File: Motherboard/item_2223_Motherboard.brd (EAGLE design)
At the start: 160 x 100 mm, 50 parts, among them IC1 MCP602SN, IC2 LD117AS33TR, IC4 MCP6S26, U1 ESP32-DEVKITC-32D, U2 ADS1256_BOARD, U3 SSD1306_128X64, X1 MSTBA4, X2 MSTBA4

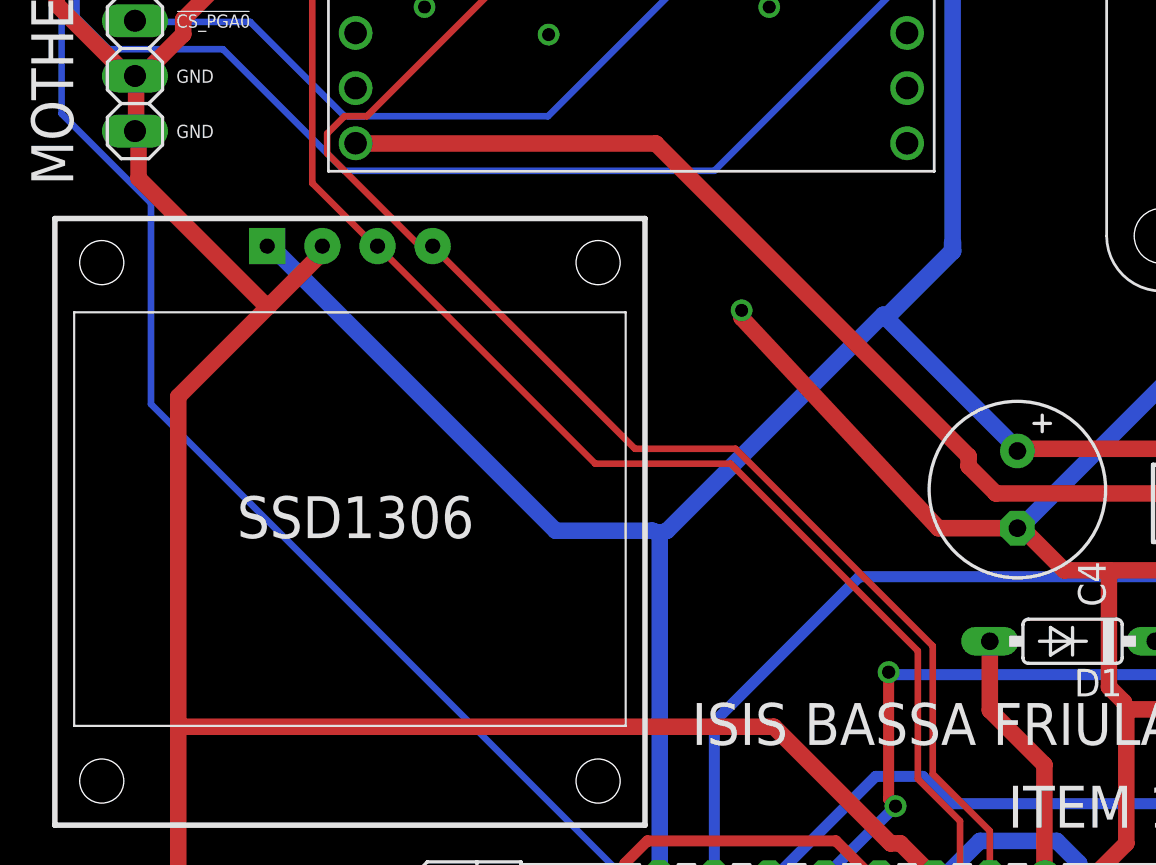
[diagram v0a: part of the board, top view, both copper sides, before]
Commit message: Corretto GND di SSD1306 in Frontend e Motherboard
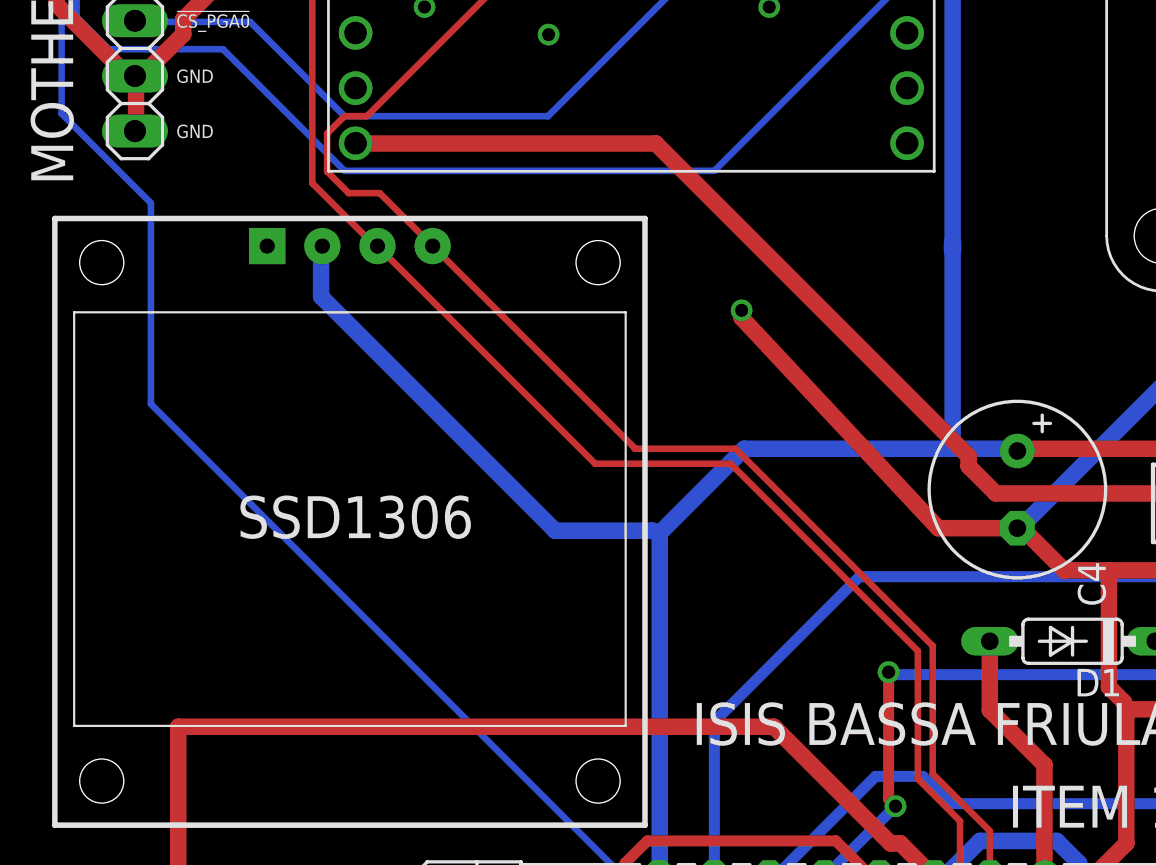
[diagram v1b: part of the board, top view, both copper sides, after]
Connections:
- net +3V3: now also U3.2; no longer U3.VCC
- net GND: now also U3.1; no longer U3.GND
- net I2C_SCL: now also U3.3; no longer U3.SCL
- net I2C_SDA: now also U3.4; no longer U3.SDA
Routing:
- net GND: track 792.6 -> 757.4 mm
- net +3V3: track 249.1 -> 247.7 mm
- net I2C_SDA: track 94.1 -> 94.6 mm
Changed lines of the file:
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@@
 <?xml version="1.0" encoding="utf-8"?>
 <!DOCTYPE eagle SYSTEM "eagle.dtd">
-<eagle version="9.6.2">
+<eagle version="7.7.0">
 <drawing>
 <settings>
 <setting alwaysvectorfont="no"/>
-<setting keepoldvectorfont="yes"/>
 <setting verticaltext="up"/>
 </settings>
@@
 <param name="dpMaxLengthDifference" value="10mm"/>
 <param name="dpGapFactor" value="2.5"/>
+<param name="checkGrid" value="0"/>
 <param name="checkAngle" value="0"/>
 <param name="checkFont" value="1"/>
 <param name="checkRestrict" value="1"/>
-<param name="checkStop" value="0"/>
-<param name="checkValues" value="0"/>
-<param name="checkNames" value="1"/>
-<param name="checkWireStubs" value="1"/>
-<param name="checkPolygonWidth" value="0"/>
 <param name="useDiameter" value="13"/>
 <param name="maxErrors" value="50"/>
@@
 <contactref element="RTD1" pad="P3"/>
 <contactref element="RTD2" pad="P3"/>
-<contactref element="U3" pad="VCC"/>
+<contactref element="U3" pad="2"/>
 <contactref element="JP1" pad="2"/>
 <contactref element="IC2" pad="4"/>
@@
 <wire x1="30.5181" y1="27.2034" x2="30.5181" y2="11.43" width="0.762" layer="16"/>
 <wire x1="30.5181" y1="11.43" x2="30.48" y2="11.43" width="0.762" layer="16"/>
-<wire x1="12.6873" y1="40.3479" x2="12.4587" y2="40.3479" width="0.762" layer="16"/>
-<wire x1="25.7175" y1="27.3177" x2="12.6873" y2="40.3479" width="0.762" layer="16"/>
-<wire x1="30.1752" y1="27.3177" x2="25.7175" y2="27.3177" width="0.762" layer="16"/>
-<wire x1="12.4587" y1="40.3479" x2="12.44" y2="40.425" width="0.762" layer="16"/>
+<wire x1="30.1752" y1="27.3177" x2="25.7048" y2="27.3177" width="0.762" layer="16"/>
 <wire x1="30.1752" y1="27.3177" x2="30.5181" y2="27.2034" width="0.762" layer="16"/>
 <wire x1="133.6167" y1="94.5261" x2="133.6167" y2="94.9833" width="0.762" layer="16"/>
@@
 <via x="128.8161" y="89.7255" extent="1-16" drill="0.6096"/>
 <via x="71.2089" y="90.4113" extent="1-16" drill="0.6096"/>
-<wire x1="30.861" y1="27.3177" x2="40.8051" y2="37.2618" width="0.762" layer="16"/>
-<wire x1="30.861" y1="27.3177" x2="30.5181" y2="27.2034" width="0.762" layer="16"/>
-<wire x1="40.8051" y1="37.2618" x2="40.93845" y2="37.12845" width="0.762" layer="16"/>
-<wire x1="40.93845" y1="37.12845" x2="46.9773" y2="31.0896" width="0.762" layer="16"/>
 <wire x1="46.9773" y1="31.0896" x2="46.99" y2="30.988" width="0.762" layer="16"/>
 <wire x1="56.5785" y1="31.7754" x2="66.6369" y2="31.7754" width="0.762" layer="1"/>
@@
 <wire x1="56.2356" y1="31.5468" x2="56.515" y2="31.725" width="0.762" layer="1"/>
 <wire x1="44.0055" y1="40.5892" x2="44.0055" y2="40.1955" width="0.8128" layer="16"/>
-<wire x1="44.0055" y1="40.1955" x2="40.93845" y2="37.12845" width="0.8128" layer="16"/>
 <contactref element="IC4" pad="14"/>
 <contactref element="C10" pad="1"/>
@@
 <wire x1="80.01" y1="30.21" x2="83.55" y2="30.21" width="0.762" layer="1"/>
 <wire x1="83.55" y1="30.21" x2="85.09" y2="31.75" width="0.762" layer="1"/>
+<wire x1="25.7048" y1="27.3177" x2="14.9225" y2="38.1" width="0.762" layer="16"/>
+<wire x1="14.9225" y1="38.1" x2="14.9225" y2="40.3675" width="0.762" layer="16"/>
+<wire x1="14.9225" y1="40.3675" x2="14.98" y2="40.425" width="0.762" layer="16"/>
+<wire x1="46.9773" y1="31.0896" x2="44.1325" y2="31.0896" width="0.762" layer="16"/>
+<wire x1="44.1325" y1="31.0896" x2="34.4043" y2="31.0896" width="0.762" layer="16"/>
+<wire x1="34.4043" y1="31.0896" x2="30.5181" y2="27.2034" width="0.762" layer="16"/>
+<wire x1="44.0055" y1="40.1955" x2="44.0055" y2="31.2166" width="0.762" layer="16"/>
+<wire x1="44.0055" y1="31.2166" x2="44.1325" y2="31.0896" width="0.762" layer="16"/>
 <wire x1="85.09" y1="31.75" x2="85.09" y2="32.2834" width="0" layer="19" extent="1-1"/>
 </signal>
@@
 <contactref element="U1" pad="26"/>
 <contactref element="U1" pad="20"/>
-<contactref element="U3" pad="GND"/>
+<contactref element="U3" pad="1"/>
 <contactref element="JP1" pad="4"/>
 <contactref element="C3" pad="2"/>
@@
 <contactref element="PL1" pad="5"/>
 <contactref element="PL1" pad="14"/>
-<wire x1="8.3439" y1="33.4899" x2="8.3439" y2="18.288" width="0.762" layer="1"/>
 <wire x1="8.3439" y1="18.288" x2="8.3439" y2="9.6012" width="0.762" layer="1"/>
-<wire x1="14.9733" y1="40.1193" x2="12.4587" y2="37.6047" width="0.762" layer="1"/>
-<wire x1="12.4587" y1="37.6047" x2="8.3439" y2="33.4899" width="0.762" layer="1"/>
-<wire x1="14.9733" y1="40.3479" x2="14.9733" y2="40.1193" width="0.762" layer="1"/>
 <wire x1="8.3439" y1="9.6012" x2="8.255" y2="9.525" width="0.762" layer="1"/>
-<wire x1="14.9733" y1="40.3479" x2="14.98" y2="40.425" width="0.762" layer="1"/>
 <wire x1="41.9481" y1="76.1238" x2="41.9481" y2="75.6666" width="0.762" layer="1"/>
 <wire x1="43.5483" y1="77.724" x2="41.9481" y2="76.1238" width="0.762" layer="1"/>
@@
 <wire x1="41.6052" y1="75.438" x2="41.91" y2="75.64" width="0.762" layer="1"/>
 <wire x1="16.8021" y1="58.0644" x2="16.51" y2="57.86" width="0.762" layer="1"/>
-<wire x1="6.5151" y1="43.5483" x2="12.4587" y2="37.6047" width="0.762" layer="1"/>
-<wire x1="6.5151" y1="45.3771" x2="6.5151" y2="43.5483" width="0.762" layer="1"/>
 <wire x1="6.5151" y1="45.3771" x2="6.35" y2="45.72" width="0.762" layer="1"/>
 <wire x1="106.299" y1="95.5548" x2="106.0704" y2="95.5548" width="0.762" layer="16"/>
@@
 <signal name="I2C_SCL" class="2">
 <contactref element="U1" pad="22"/>
-<contactref element="U3" pad="SCL"/>
+<contactref element="U3" pad="3"/>
 <contactref element="PL1" pad="4"/>
 <wire x1="45.72" y1="9.7155" x2="45.72" y2="8.89" width="0.3048" layer="1"/>
@@
 <wire x1="42.4053" y1="21.7805" x2="42.4053" y2="15.8877" width="0.3048" layer="1"/>
 <wire x1="33.782" y1="30.4038" x2="42.4053" y2="21.7805" width="0.3048" layer="1"/>
-<wire x1="27.5463" y1="30.4038" x2="33.782" y2="30.4038" width="0.3048" layer="1"/>
-<wire x1="17.6022" y1="40.3479" x2="27.5463" y2="30.4038" width="0.3048" layer="1"/>
-<wire x1="17.6022" y1="40.3479" x2="17.52" y2="40.425" width="0.3048" layer="1"/>
+<wire x1="27.5412" y1="30.4038" x2="33.782" y2="30.4038" width="0.3048" layer="1"/>
 <wire x1="41.8338" y1="85.0392" x2="41.8338" y2="85.725" width="0.3048" layer="1"/>
 <wire x1="25.4889" y1="68.6943" x2="41.8338" y2="85.0392" width="0.3048" layer="1"/>
@@
 <wire x1="17.3736" y1="40.4622" x2="14.5161" y2="43.3197" width="0.3048" layer="1"/>
 <wire x1="41.8338" y1="85.725" x2="41.91" y2="85.8" width="0.3048" layer="1"/>
-<wire x1="17.3736" y1="40.4622" x2="17.52" y2="40.425" width="0.3048" layer="1"/>
 <via x="25.4889" y="63.0936" extent="1-16" drill="0.6096"/>
 <via x="18.1737" y="55.2069" extent="1-16" drill="0.6096"/>
+<wire x1="27.5412" y1="30.4038" x2="17.52" y2="40.425" width="0.3048" layer="1"/>
+<wire x1="17.52" y1="40.425" x2="17.3736" y2="40.4622" width="0" layer="19" extent="1-1"/>
 </signal>
 <signal name="I2C_SDA" class="2">
 <contactref element="U1" pad="25"/>
-<contactref element="U3" pad="SDA"/>
+<contactref element="U3" pad="4"/>
 <contactref element="PL1" pad="3"/>
 <wire x1="45.72" y1="13.4874" x2="45.72" y2="11.43" width="0.3048" layer="1"/>
@@
 <wire x1="34.0106" y1="31.0896" x2="43.0911" y2="22.0091" width="0.3048" layer="1"/>
 <wire x1="29.3751" y1="31.0896" x2="34.0106" y2="31.0896" width="0.3048" layer="1"/>
-<wire x1="20.1168" y1="40.3479" x2="29.3751" y2="31.0896" width="0.3048" layer="1"/>
-<wire x1="20.1168" y1="40.3479" x2="20.06" y2="40.425" width="0.3048" layer="1"/>
 <wire x1="26.8605" y1="63.0936" x2="41.8338" y2="78.0669" width="0.3048" layer="1"/>
 <wire x1="26.8605" y1="56.2356" x2="26.8605" y2="63.0936" width="0.3048" layer="16"/>
@@
 <wire x1="16.002" y1="46.4058" x2="17.0307" y2="46.4058" width="0.3048" layer="1"/>
 <wire x1="15.2019" y1="45.6057" x2="16.002" y2="46.4058" width="0.3048" layer="1"/>
-<wire x1="15.2019" y1="44.6913" x2="15.2019" y2="45.6057" width="0.3048" layer="1"/>
-<wire x1="19.431" y1="40.4622" x2="15.2019" y2="44.6913" width="0.3048" layer="1"/>
-<wire x1="20.0025" y1="40.4622" x2="19.431" y2="40.4622" width="0.3048" layer="1"/>
+<wire x1="15.2019" y1="43.8531" x2="15.2019" y2="45.6057" width="0.3048" layer="1"/>
 <wire x1="41.8338" y1="78.0669" x2="41.91" y2="78.18" width="0.3048" layer="1"/>
-<wire x1="20.0025" y1="40.4622" x2="20.06" y2="40.425" width="0.3048" layer="1"/>
 <via x="26.8605" y="63.0936" extent="1-16" drill="0.6096"/>
 <via x="26.8605" y="56.2356" extent="1-16" drill="0.6096"/>
+<wire x1="29.3751" y1="31.0896" x2="29.3751" y2="31.1099" width="0.3048" layer="1"/>
+<wire x1="29.3751" y1="31.1099" x2="20.06" y2="40.425" width="0.3048" layer="1"/>
+<wire x1="15.2019" y1="43.8531" x2="16.1925" y2="42.8625" width="0.3048" layer="1"/>
+<wire x1="16.1925" y1="42.8625" x2="17.6225" y2="42.8625" width="0.3048" layer="1"/>
+<wire x1="17.6225" y1="42.8625" x2="20.06" y2="40.425" width="0.3048" layer="1"/>
 </signal>
 <signal name="ADC_HALF_VREF" class="1">
@@
 </signal>
 </signals>
-<mfgpreviewcolors>
-<mfgpreviewcolor name="soldermaskcolor" color="0xC8008000"/>
-<mfgpreviewcolor name="silkscreencolor" color="0xFFFEFEFE"/>
-<mfgpreviewcolor name="backgroundcolor" color="0xFF282828"/>
-<mfgpreviewcolor name="coppercolor" color="0xFFFFBF00"/>
-<mfgpreviewcolor name="substratecolor" color="0xFF786E46"/>
-</mfgpreviewcolors>
 </board>
 </drawing>

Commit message: ingresso differenziale e AGND
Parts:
- added C12, C13, C15: 100nF, rcl_LargePads:C0805
- added C14: 10uF / 16V, rcl_LargePads:PANASONIC_C
- added IC3: MCP1525TO, MCP1525_MCP1541:TO92
- added IC5: MCP6004SO, MCP6002_MCP6004:SO14
- added IC7: LM336LP, linear:TO92
- added R10, R11: 6.8k, rcl_LargePads:R0805
- added R31: 2.7k, rcl:R0805
- added SJ1: (no value), jumper:SJ
- added TP7, TP8: TPTP16R, testpad:TP16R
- JP1: device pinhead:1X08 -> pinhead:1X10
- moved JP1 193.2 mm to (8.26, -46.4)
- moved TP9 122.6 mm to (-3.81, -50.8)
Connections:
- removed net AIN0-: C9.1, R9.2, U2.AIN0-
- new net +2.5V: IC5.1, IC5.2, JP1.1
- new net ADC_HALF_VREF_B: IC5.13, IC5.14
- new net ADC_VREF: IC5.6, IC5.7, JP1.2, TP9.TP
- new net AGND: C10.2, C11.2, C12.2, C13.2, C14.-, C15.2, C5.2, C7.2, C9.2, IC3.1, IC4.9, IC5.11, IC7.3, JP1.4, R11.1, SJ1.2, X1.1, X1.4, X2.1, X2.4
- new net AIN1+: C9.1, R9.1, U2.AIN1+
- new net N$1: C15.1, IC5.10, IC5.12, R10.1, R11.2
- new net VREF: C14.+, IC3.2, IC5.3, IC5.5, IC7.2, R10.2, R31.1, TP7.TP
- net !CS_MCP3204!: now also JP1.7; no longer JP1.5
- net +3V3: now also JP1.5; no longer JP1.2
- net +5V: now also C12.1, C13.1, IC3.3, IC5.4, R31.2
- net ADC_HALF_VREF: now also IC5.8, IC5.9, R9.2, TP8.TP; no longer JP1.1, TP9.TP
- net GND: now also JP1.6, SJ1.1; no longer C10.2, C11.2, C5.2, C7.2, C9.2, IC4.9, JP1.4, R9.1, X1.1, X1.4, X2.1, X2.4
- net VSPI_MISO: now also JP1.9; no longer JP1.7
- net VSPI_MOSI: now also JP1.10; no longer JP1.8
- net VSPI_SCK: now also JP1.8; no longer JP1.6
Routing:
- net GND: track 757.4 -> 689.3 mm, vias 28 -> 27
- net AIN0-: track 9.02 -> 0.00 mm
